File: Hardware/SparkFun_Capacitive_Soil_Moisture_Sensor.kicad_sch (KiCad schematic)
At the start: 28 parts, among them J1 Qwiic_RA, J2 Qwiic_RA, U1 CY8CMBR3102

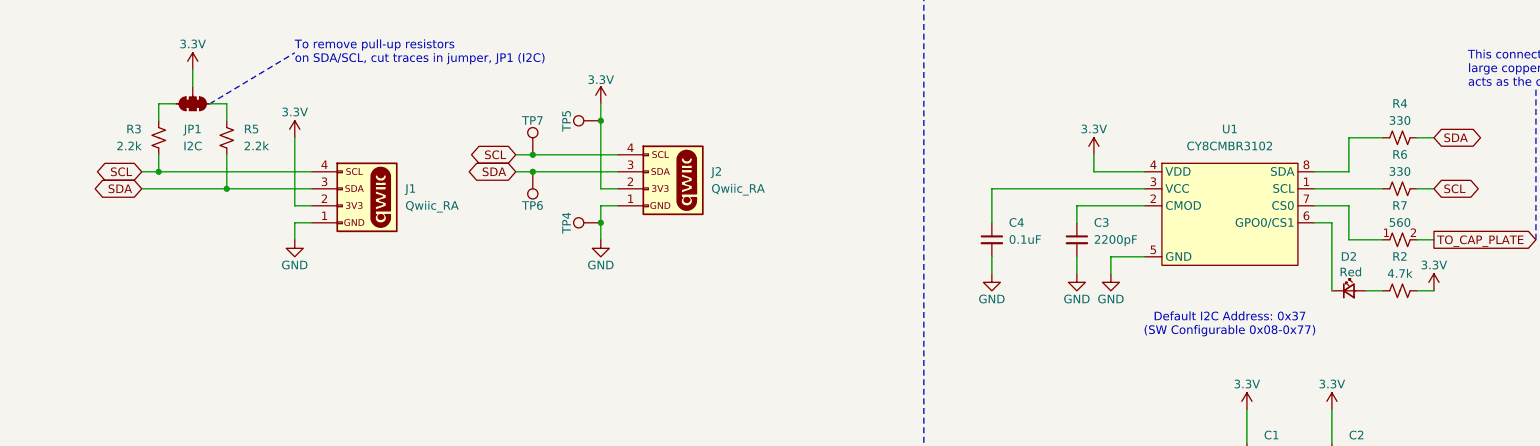
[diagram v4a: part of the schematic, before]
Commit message: Update PCB with new CY8CMBR3 IC
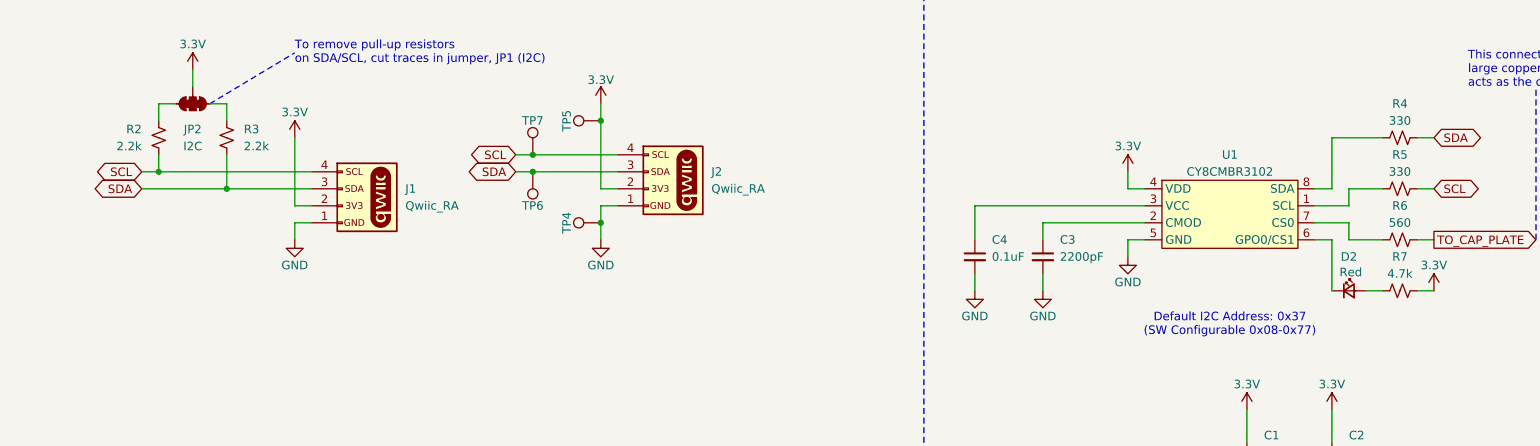
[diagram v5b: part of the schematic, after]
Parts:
- removed C3: 2200pF, SparkFun-Capacitor:C_0402_1005Metric, symbol SparkFun-Capacitor:2200pF_0402_50V_10%
- added C3: 2200pF, SparkFun-Capacitor:C_0603_1608Metric, symbol SparkFun-Capacitor:2200pF_0603_50V_10%
- renumbered JP1 to JP2, R3 to R2, R5 to R3, R6 to R5, R7 to R6, R2 to R7
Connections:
- net GND: now also C3.2
- net at U1.2 (CMOD): now also C3.1
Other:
- moved on the sheet: C4

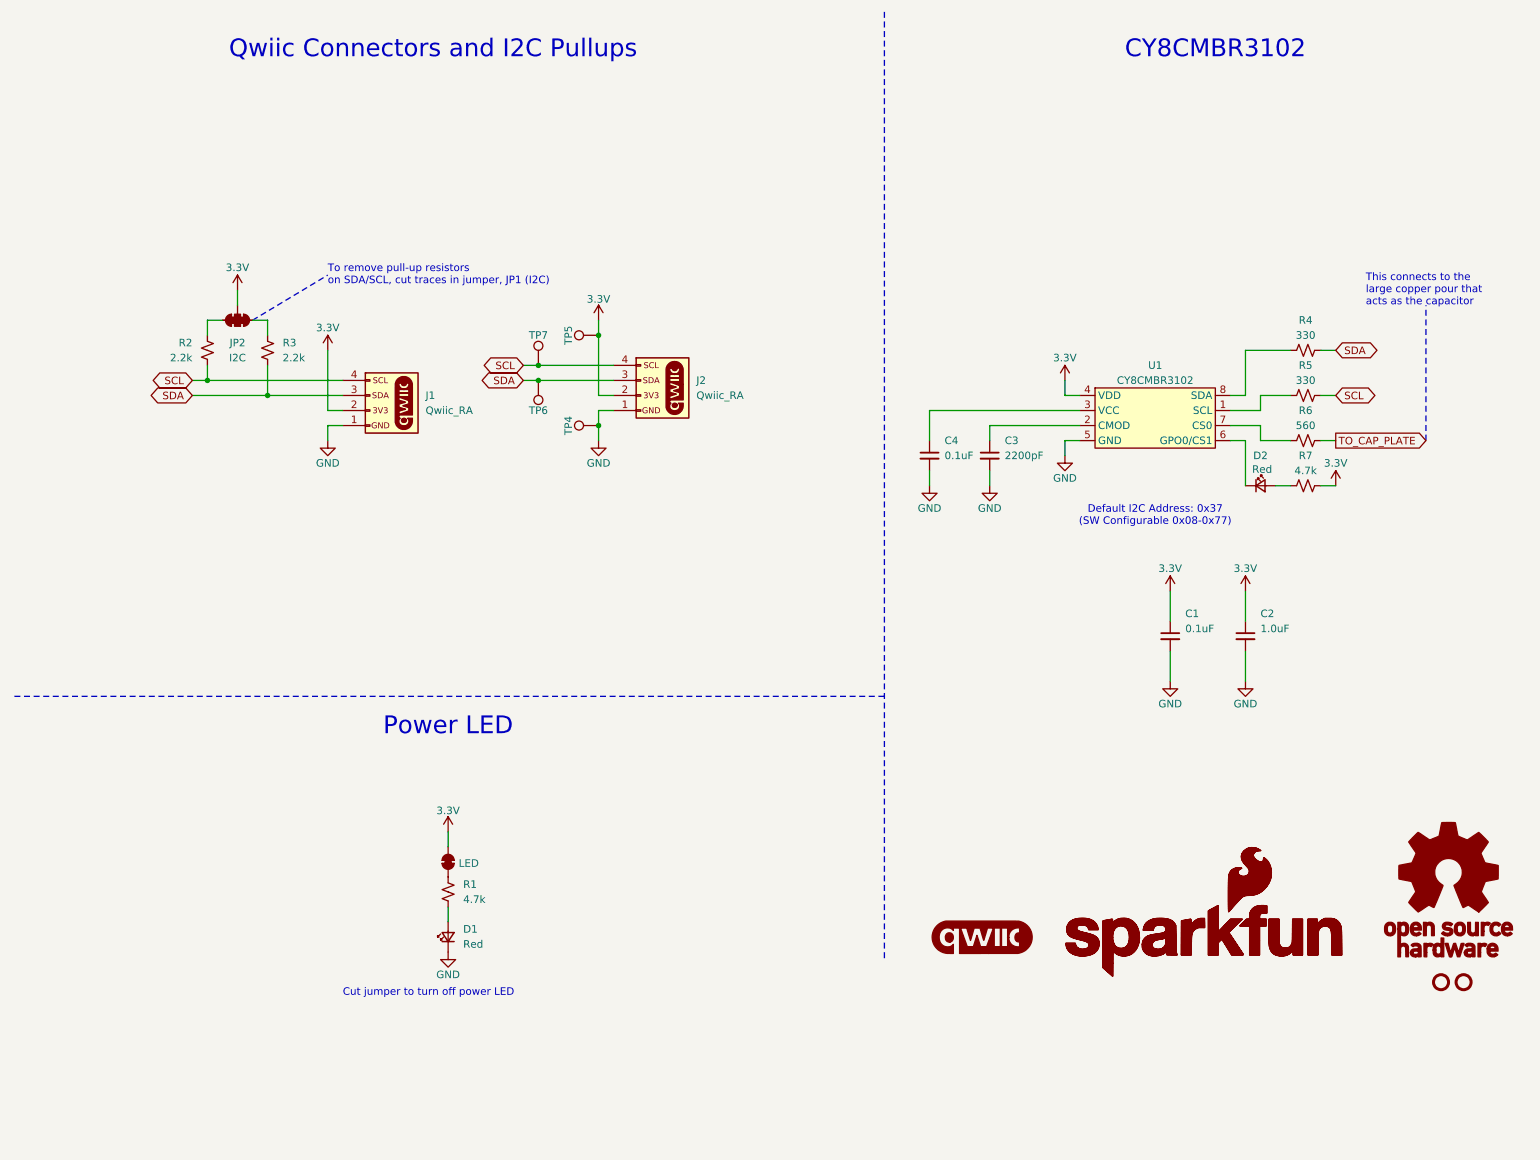
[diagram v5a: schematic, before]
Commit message: Fix sizing and naming in schematic based on review
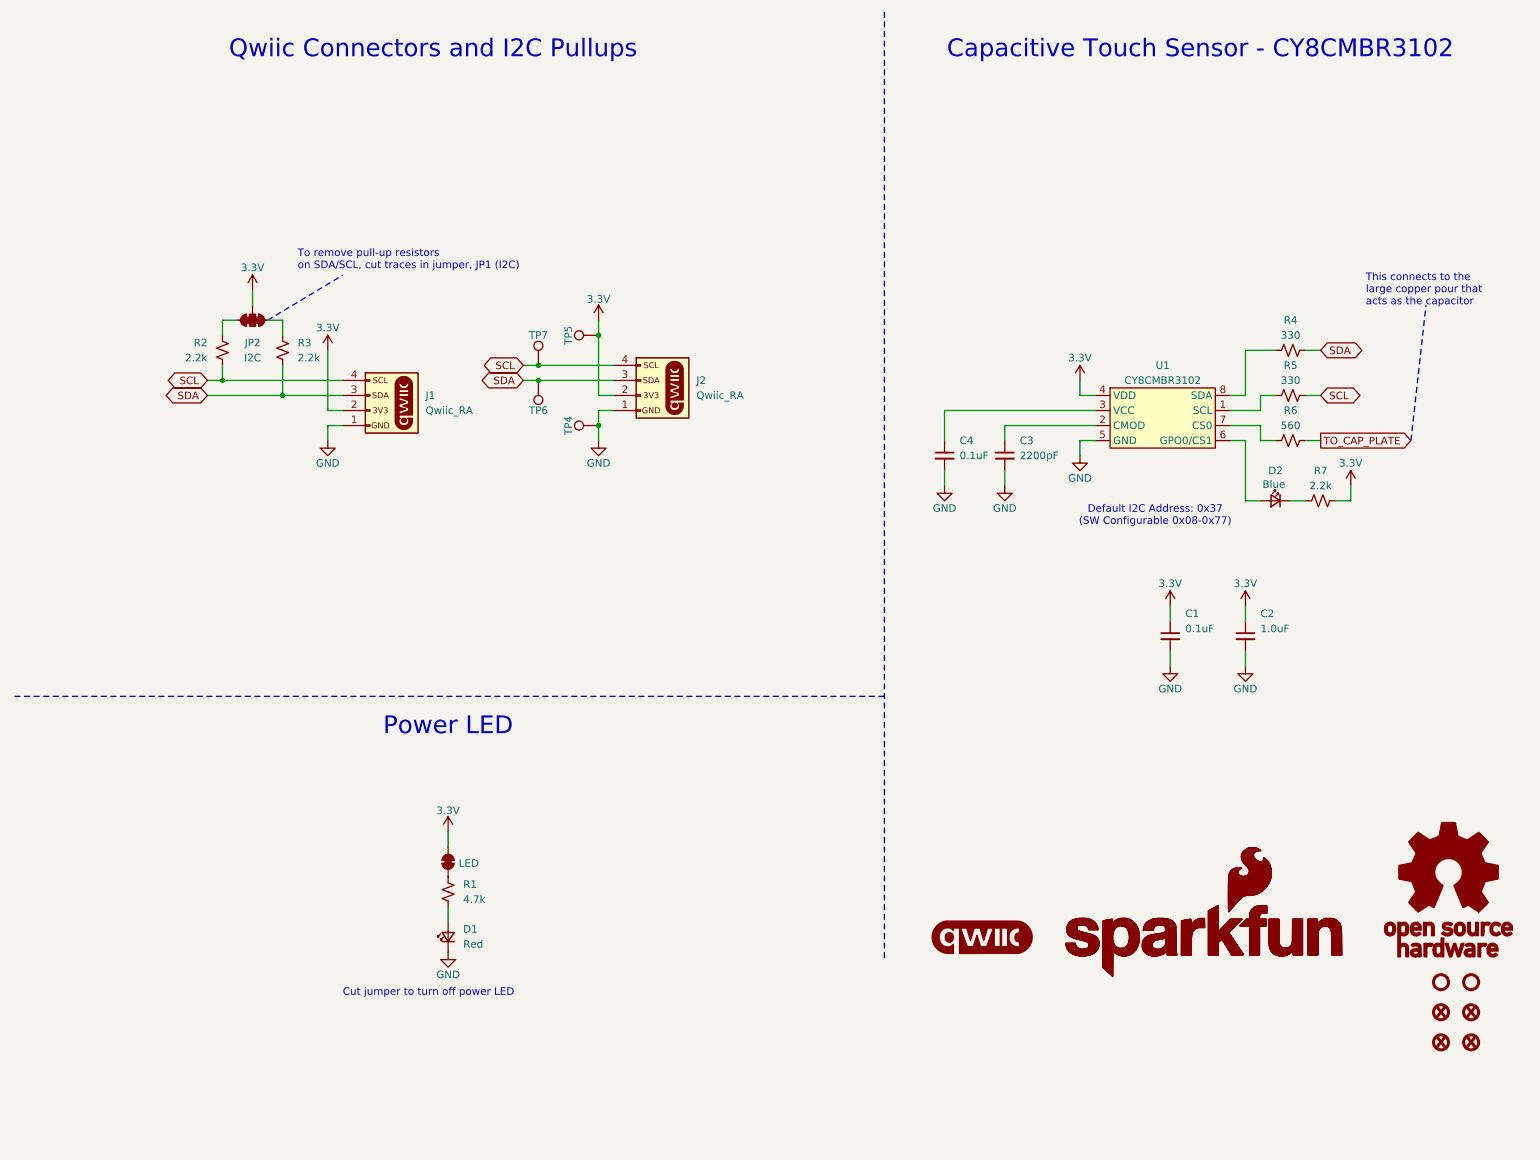
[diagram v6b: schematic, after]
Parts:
- added FID1, FID2, FID3, FID4: Fiducial_0.5mm, SparkFun-Aesthetic:Fiducial_0.5mm_Mask1mm, symbol SparkFun-Aesthetic:Fiducial_0.5mm
- C3: PROD_ID TODO: PROD_ID -> CAP-27514
- D2: value Red -> Blue; footprint SparkFun-LED:LED_0603_1608Metric_Red -> SparkFun-LED:LED_0603_1608Metric_Blue; symbol SparkFun-LED:LED_Red_0603 -> SparkFun-LED:LED_Blue_0603; PROD_ID DIO-17976 -> DIO-08575
- R6: PROD_ID TODO:PROD_ID -> RES-27513
- R7: value 4.7k -> 2.2k; symbol SparkFun-Resistor:4.7k_0603 -> SparkFun-Resistor:2.2k_0603; PROD_ID RES-07857 -> RES-08272
- U1: PROD_ID TODO: PROD_ID -> IC-27515
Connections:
- net at U1.6 (GPO0/CS1): now also D2.2 (A); no longer D2.1 (K)
- net at R7.2: now also D2.1 (K); no longer D2.2 (A)
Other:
- note added: "Capacitive Touch Sensor - CY8CMBR3102"
- note removed: "CY8CMBR3102"
- moved on the sheet: C3, C4, D2, JP2, R2, R3, R4, R5, R6, R7, U1

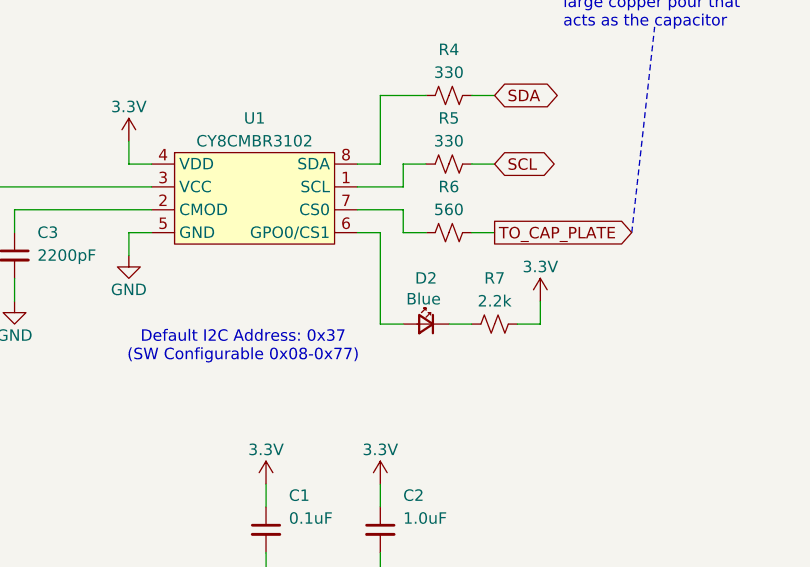
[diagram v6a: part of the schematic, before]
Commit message: Add PCB fixes from review
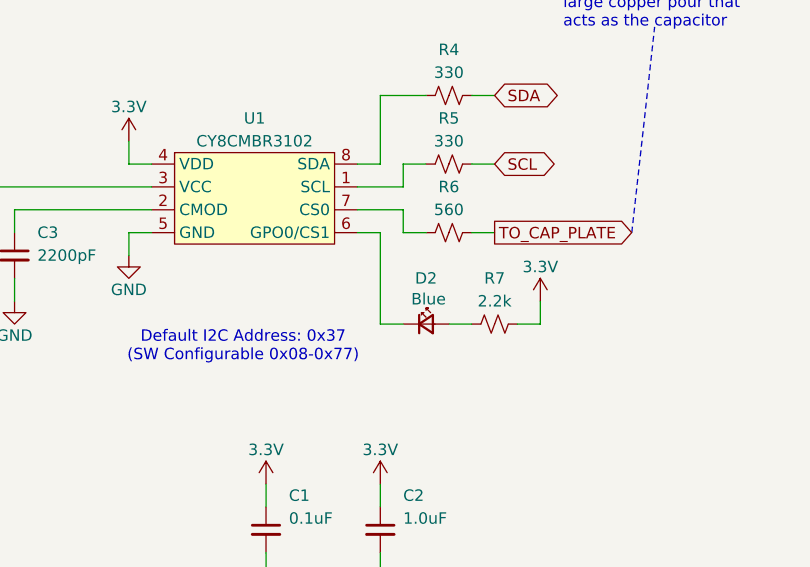
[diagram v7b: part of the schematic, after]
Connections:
- net at U1.6 (GPO0/CS1): now also D2.1 (K); no longer D2.2 (A)
- net at R7.2: now also D2.2 (A); no longer D2.1 (K)
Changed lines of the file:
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@@
+	(wire
+		(pts
+			(xy 220.98 93.98) (xy 220.98 83.82)
+		)
+		(stroke
+			(width 0)
+			(type default)
+		)
+	)
+	(wire
+		(pts
+			(xy 228.6 93.98) (xy 231.14 93.98)
+		)
+		(stroke
+			(width 0)
+			(type default)
+		)
+	)
 	(wire
 		(pts
@@
 	(wire
 		(pts
+			(xy 223.52 93.98) (xy 220.98 93.98)
+		)
+		(stroke
+			(width 0)
+			(type default)
+		)
+	)
+	(wire
+		(pts
 			(xy 101.6 71.12) (xy 114.3 71.12)
 		)
@@
 	(wire
 		(pts
+			(xy 220.98 83.82) (xy 218.44 83.82)
+		)
+		(stroke
+			(width 0)
+			(type default)
+		)
+	)
+	(wire
+		(pts
 			(xy 68.58 81.28) (xy 66.04 81.28)
 		)
@@
 		(pts
 			(xy 236.22 93.98) (xy 238.76 93.98)
-		)
-		(stroke
-			(width 0)
-			(type default)
-		)
-	)
-	(wire
-		(pts
-			(xy 220.98 93.98) (xy 223.52 93.98)
 		)
 		(stroke
@@
 		)
 	)
-	(wire
-		(pts
-			(xy 220.98 83.82) (xy 220.98 93.98)
-		)
-		(stroke
-			(width 0)
-			(type default)
-		)
-	)
 	(polyline
 		(pts
@@
 	(wire
 		(pts
-			(xy 228.6 93.98) (xy 231.14 93.98)
-		)
-		(stroke
-			(width 0)
-			(type default)
-		)
-	)
-	(wire
-		(pts
 			(xy 66.04 78.74) (xy 66.04 68.58)
 		)
@@
 			(type dash)
 			(color 132 132 132 1)
-		)
-	)
-	(wire
-		(pts
-			(xy 218.44 83.82) (xy 220.98 83.82)
-		)
-		(stroke
-			(width 0)
-			(type default)
 		)
 	)
@@
 		(lib_id "SparkFun-LED:LED_Blue_0603")
 		(at 226.06 93.98 0)
-		(mirror y)
 		(unit 1)
 		(exclude_from_sim no)
@@
 		)
 		(property "Value" "Blue"
-			(at 225.7816 91.2109 0)
-			(effects
-				(font
+			(at 226.3384 91.2109 0)
+			(effects
+				(font

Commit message: Update cap to correct prod_id
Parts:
- C3: PROD_ID CAP-27514 -> CAP-07877
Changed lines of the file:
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@@
 			)
 		)
-		(property "Datasheet" "https://jlcpcb.com/api/file/downloadByFileSystemAccessId/8588930837694337024"
+		(property "Datasheet" "https://www.niccomp.com/wp-content/uploads/catalog/nmc2.pdf"
 			(at 180.34 102.87 0)
 			(effects
@@
 			)
 		)
-		(property "PROD_ID" "CAP-27514"
+		(property "PROD_ID" "CAP-07877"
 			(at 180.34 100.33 0)
 			(effects
